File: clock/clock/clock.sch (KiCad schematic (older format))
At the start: 43 parts, among them J1 AVR-ISP-6, J10 Conn_01x05_Male, J11 Conn_01x05_Male, J12 Conn_01x05_Male, J13 Conn_01x05_Male, J2 EURORACK_CONN_10, J3 CV_IN, J4 CLOCK_OUT, J5 SUBDIV_OUT, J6 Conn_01x05_Female, J7 Conn_01x05_Female, J8 Conn_01x05_Female, J9 Conn_01x05_Female, SW1 SW_Push, SW2 SW_Push, SW3 SW_Rotary8, U1 ATmega328P-PU, U2 L7805, U3 SM460281N, U4 SM460281N, U5 SM460281N, Y1 16MHz

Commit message: pcb layout first pass
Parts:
- renumbered J13 to J10, J3 to J11, J4 to J12, J5 to J13, J6 to J3, J10 to J4, J7 to J5, J11 to J6, J8 to J7, J12 to J8
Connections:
- net +5V: now also J9.3 (Pin_3); no longer J7.4 (Pin_4)
- net AGND: now also J10.4 (Pin_4), R4.2, R5.2; no longer J13.S, J8.5 (Pin_5)
- net AVCC: now also J10.3 (Pin_3); no longer J8.4 (Pin_4)
- net B_CLOCK_OUT: now also J3.3 (Pin_3); no longer J3.1 (Pin_1)
- net B_CV_IN: now also J3.1 (Pin_1); no longer J3.3 (Pin_3)
- net B_LED0: now also J3.5 (Pin_5); no longer J3.4 (Pin_4)
- net B_LED1: now also J5.3 (Pin_3); no longer J3.5 (Pin_5)
- net B_LED3: now also J5.4 (Pin_4); no longer J5.2 (Pin_2)
- net B_LED4: now also J7.1 (Pin_1); no longer J5.3 (Pin_3)
- net B_LED5: now also J7.2 (Pin_2); no longer J5.4 (Pin_4)
- net B_LED6: now also J7.3 (Pin_3); no longer J5.5 (Pin_5)
- net B_LED_A: now also J7.4 (Pin_4); no longer J9.3 (Pin_3)
- net B_LED_B: now also J7.5 (Pin_5); no longer J9.4 (Pin_4)
- net B_LED_C1: now also J3.4 (Pin_4); no longer J7.1 (Pin_1)
- net B_LED_C2: now also J5.2 (Pin_2); no longer J7.2 (Pin_2)
- net B_LED_C3: now also J5.5 (Pin_5); no longer J7.3 (Pin_3)
- net CLOCK_OUT: now also J4.3 (Pin_3); no longer J4.1 (Pin_1)
- net CV_IN: now also J4.1 (Pin_1); no longer J4.3 (Pin_3)
- net GND: now also J9.4 (Pin_4); no longer J7.5 (Pin_5), R4.2, R5.2
- net LED0: now also U4.3 (G); no longer U4.4 (E)
- net LED1: now also U4.4 (E); no longer U4.2 (F)
- net LED2: now also U4.2 (F); no longer U4.3 (G)
- net LED_A: now also J8.4 (Pin_4); no longer J10.3 (Pin_3)
- net LED_B: now also J8.5 (Pin_5); no longer J10.4 (Pin_4)
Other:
- note added: "NOTE: this weird wiring is\nfor layout optimization"
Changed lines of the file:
@@
 $EndComp
 $Comp
-L Connector:AudioJack2 J4
+L Connector:AudioJack2 J12
 U 1 1 6321922B
 P 6750 5600
-F 0 "J4" H 6570 5583 50  0000 R CNN
+F 0 "J12" H 6570 5583 50  0000 R CNN
 F 1 "CLOCK_OUT" H 6570 5674 50  0000 R CNN
 F 2 "synth:Jack_3.5mm_QingPu_WQP-PJ398SM_Vertical_CircularHoles" H 6750 5600 50  0001 C CNN
@@
 $EndComp
 $Comp
-L Connector:AudioJack2 J5
+L Connector:AudioJack2 J13
 U 1 1 6321A6EF
 P 6750 6150
-F 0 "J5" H 6570 6133 50  0000 R CNN
+F 0 "J13" H 6570 6133 50  0000 R CNN
 F 1 "SUBDIV_OUT" H 6570 6224 50  0000 R CNN
 F 2 "synth:Jack_3.5mm_QingPu_WQP-PJ398SM_Vertical_CircularHoles" H 6750 6150 50  0001 C CNN
@@
 	1    0    0    -1
 $EndComp
-$Comp
-L power:GND #PWR015
-U 1 1 63227A93
-P 4100 6250
-F 0 "#PWR015" H 4100 6000 50  0001 C CNN
-F 1 "GND" H 4105 6077 50  0000 C CNN
-F 2 "" H 4100 6250 50  0001 C CNN
-F 3 "" H 4100 6250 50  0001 C CNN
-	1    4100 6250
-	1    0    0    -1
-$EndComp
 Wire Wire Line
 	4100 6250 4100 6100
@@
 	6850 2300 6850 1350
 Connection ~ 6850 1350
-Wire Wire Line
-	6750 1250 8400 1250
 Connection ~ 6750 1250
 Connection ~ 6650 1150
@@
 	11150 2500 11100 2500
 Wire Wire Line
-	8400 1250 10050 1250
-Wire Wire Line
 	8000 850  9650 850
 Connection ~ 8000 850
-Connection ~ 8400 1250
 Wire Wire Line
 	9500 2500 9500 2800
@@
 	1    0    0    -1
 $EndComp
-$Comp
-L power:GND #PWR018
-U 1 1 63552A08
-P 5250 6250
-F 0 "#PWR018" H 5250 6000 50  0001 C CNN
-F 1 "GND" H 5255 6077 50  0000 C CNN
-F 2 "" H 5250 6250 50  0001 C CNN
-F 3 "" H 5250 6250 50  0001 C CNN
-	1    5250 6250
-	1    0    0    -1
-$EndComp
 Wire Wire Line
 	5250 6250 5250 6100
@@
 B_SW2
 $Comp
-L Connector:AudioJack2 J3
+L Connector:AudioJack2 J11
 U 1 1 6328406C
 P 6750 5200
-F 0 "J3" H 6570 5183 50  0000 R CNN
+F 0 "J11" H 6570 5183 50  0000 R CNN
 F 1 "CV_IN" H 6570 5274 50  0000 R CNN
 F 2 "synth:Jack_3.5mm_QingPu_WQP-PJ398SM_Vertical_CircularHoles" H 6750 5200 50  0001 C CNN
@@
 	1000 2650 1250 2650
 $Comp
-L Connector:Conn_01x05_Male J10
+L Connector:Conn_01x05_Male J4
 U 1 1 63323658
 P 10200 3900
-F 0 "J10" H 10308 4281 50  0000 C CNN
+F 0 "J4" H 10308 4281 50  0000 C CNN
 F 1 "Conn_01x05_Male" V 10100 4000 50  0000 C CNN
 F 2 "Connector_PinHeader_2.54mm:PinHeader_1x05_P2.54mm_Vertical" H 10200 3900 50  0001 C CNN
@@
 $EndComp
 $Comp
-L Connector:Conn_01x05_Female J6
+L Connector:Conn_01x05_Female J3
 U 1 1 63325045
 P 9800 3900
-F 0 "J6" H 9650 4300 50  0000 L CNN
+F 0 "J3" H 9650 4300 50  0000 L CNN
 F 1 "Conn_01x05_Female" V 9850 3700 50  0000 L CNN
 F 2 "Connector_PinSocket_2.54mm:PinSocket_1x05_P2.54mm_Vertical" H 9800 3900 50  0001 C CNN
@@
 Text Label 2700 4150 0    50   ~ 0
 ~RESET
-Text Label 9500 6350 2    50   ~ 0
+Text Label 9450 5650 2    50   ~ 0
 B_LED_B
-Text Label 9500 4000 2    50   ~ 0
+Text Label 9500 4100 2    50   ~ 0
 B_LED0
-Text Label 9500 4100 2    50   ~ 0
+Text Label 9500 4650 2    50   ~ 0
 B_LED1
 Text Label 9500 4450 2    50   ~ 0
 B_LED2
-Text Label 9500 4550 2    50   ~ 0
+Text Label 9500 4750 2    50   ~ 0
 B_LED3
-Text Label 9500 4650 2    50   ~ 0
+Text Label 9500 5250 2    50   ~ 0
 B_LED4
-Text Label 9500 4750 2    50   ~ 0
+Text Label 9500 5350 2    50   ~ 0
 B_LED5
-Text Label 9500 4850 2    50   ~ 0
+Text Label 9500 5450 2    50   ~ 0
 B_LED6
 $Comp
 L power:+5V #PWR0101
 U 1 1 6334253F
-P 9000 5450
-F 0 "#PWR0101" H 9000 5300 50  0001 C CNN
-F 1 "+5V" H 9015 5623 50  0000 C CNN
-F 2 "" H 9000 5450 50  0001 C CNN
-F 3 "" H 9000 5450 50  0001 C CNN
-	1    9000 5450
+P 9050 6150
+F 0 "#PWR0101" H 9050 6000 50  0001 C CNN
+F 1 "+5V" H 9065 6323 50  0000 C CNN
+F 2 "" H 9050 6150 50  0001 C CNN
+F 3 "" H 9050 6150 50  0001 C CNN
+	1    9050 6150
 	1    0    0    -1
 $EndComp
@@
 L power:GND #PWR0102
 U 1 1 63342CA7
-P 9000 5750
-F 0 "#PWR0102" H 9000 5500 50  0001 C CNN
-F 1 "GND" H 9005 5577 50  0000 C CNN
-F 2 "" H 9000 5750 50  0001 C CNN
-F 3 "" H 9000 5750 50  0001 C CNN
-	1    9000 5750
+P 9050 6450
+F 0 "#PWR0102" H 9050 6200 50  0001 C CNN
+F 1 "GND" H 9055 6277 50  0000 C CNN
+F 2 "" H 9050 6450 50  0001 C CNN
+F 3 "" H 9050 6450 50  0001 C CNN
+	1    9050 6450
 	1    0    0    -1
 $EndComp
 Text Label 9500 6050 2    50   ~ 0
 B_KNOB
-Text Label 9500 3900 2    50   ~ 0
+Text Label 9500 3700 2    50   ~ 0
 B_CV_IN
-Text Label 9500 5250 2    50   ~ 0
+Text Label 9500 4000 2    50   ~ 0
 B_LED_C1
-Text Label 9500 5350 2    50   ~ 0
+Text Label 9500 4550 2    50   ~ 0
 B_LED_C2
-Text Label 9500 5450 2    50   ~ 0
+Text Label 9500 4850 2    50   ~ 0
 B_LED_C3
-Text Label 9500 6250 2    50   ~ 0
+Text Label 9450 5550 2    50   ~ 0
 B_LED_A
 Text Label 2700 2850 0    50   ~ 0
@@
 Text Label 9500 3800 2    50   ~ 0
 B_SUBDIV_OUT
-Text Label 9500 3700 2    50   ~ 0
+Text Label 9500 3900 2    50   ~ 0
 B_CLOCK_OUT
 $Comp
-L Connector:Conn_01x05_Male J11
+L Connector:Conn_01x05_Male J6
 U 1 1 633C2E72
 P 10200 4650
-F 0 "J11" H 10308 5031 50  0000 C CNN
+F 0 "J6" H 10308 5031 50  0000 C CNN
 F 1 "Conn_01x05_Male" V 10100 4750 50  0000 C CNN
 F 2 "Connector_PinHeader_2.54mm:PinHeader_1x05_P2.54mm_Vertical" H 10200 4650 50  0001 C CNN
@@
 $EndComp
 $Comp
-L Connector:Conn_01x05_Female J7
+L Connector:Conn_01x05_Female J5
 U 1 1 633C2E7C
 P 9800 4650
-F 0 "J7" H 9650 5050 50  0000 L CNN
+F 0 "J5" H 9650 5050 50  0000 L CNN
 F 1 "Conn_01x05_Female" V 9850 4450 50  0000 L CNN
 F 2 "Connector_PinSocket_2.54mm:PinSocket_1x05_P2.54mm_Vertical" H 9800 4650 50  0001 C CNN
@@
 $EndComp
 $Comp
-L Connector:Conn_01x05_Male J12
+L Connector:Conn_01x05_Male J8
 U 1 1 633ED584
 P 10200 5450
-F 0 "J12" H 10308 5831 50  0000 C CNN
+F 0 "J8" H 10308 5831 50  0000 C CNN
 F 1 "Conn_01x05_Male" V 10100 5550 50  0000 C CNN
 F 2 "Connector_PinHeader_2.54mm:PinHeader_1x05_P2.54mm_Vertical" H 10200 5450 50  0001 C CNN
@@
 $EndComp
 $Comp
-L Connector:Conn_01x05_Female J8
+L Connector:Conn_01x05_Female J7
 U 1 1 633ED58E
 P 9800 5450
-F 0 "J8" H 9650 5850 50  0000 L CNN
+F 0 "J7" H 9650 5850 50  0000 L CNN
 F 1 "Conn_01x05_Female" V 9850 5250 50  0000 L CNN
 F 2 "Connector_PinSocket_2.54mm:PinSocket_1x05_P2.54mm_Vertical" H 9800 5450 50  0001 C CNN
@@
 $EndComp
 $Comp
-L Connector:Conn_01x05_Male J13
+L Connector:Conn_01x05_Male J10
 U 1 1 633FDEA6
 P 10200 6250
-F 0 "J13" H 10308 6631 50  0000 C CNN
+F 0 "J10" H 10308 6631 50  0000 C CNN
 F 1 "Conn_01x05_Male" V 10100 6350 50  0000 C CNN
 F 2 "Connector_PinHeader_2.54mm:PinHeader_1x05_P2.54mm_Vertical" H 10200 6250 50  0001 C CNN
@@
 	9500 6450 9600 6450
 Wire Wire Line
-	9600 6350 9500 6350
-Wire Wire Line
-	9500 6250 9600 6250
-Wire Wire Line
-	9600 6150 9500 6150
-Wire Wire Line
 	9500 6050 9600 6050
 Wire Wire Line
-	9600 5650 9000 5650
-Wire Wire Line
-	9000 5650 9000 5750
-Wire Wire Line
-	9600 5550 9000 5550
-Wire Wire Line
-	9000 5550 9000 5450
+	9050 6350 9050 6450
+Wire Wire Line
+	9050 6250 9050 6150
 Wire Wire Line
 	9600 5450 9500 5450
@@
 Text Label 10500 5450 0    50   ~ 0
 LED6
-Text Label 10500 3900 0    50   ~ 0
+Text Label 10500 3700 0    50   ~ 0
 CV_IN
 Text Label 10500 3800 0    50   ~ 0
 SUBDIV_OUT
-Text Label 10500 3700 0    50   ~ 0
+Text Label 10500 3900 0    50   ~ 0
 CLOCK_OUT
-Text Label 10500 6350 0    50   ~ 0
+Text Label 10500 5650 0    50   ~ 0
 LED_B
 Text Label 10500 6050 0    50   ~ 0
 KNOB
-Text Label 10500 6250 0    50   ~ 0
+Text Label 10500 5550 0    50   ~ 0
 LED_A
 Text Label 10500 6150 0    50   ~ 0
@@
 Text Label 10500 4850 0    50   ~ 0
 LED_C3
-Text Label 10500 5550 0    50   ~ 0
+Text Label 10500 6250 0    50   ~ 0
 AVCC
 Text Label 6350 5700 2    50   ~ 0
@@
 Text Label 6250 3400 1    50   ~ 0
 AVCC
-Text Label 6350 6250 2    50   ~ 0
+Text Label 5250 6250 3    50   ~ 0
 AGND
 Text Label 7150 5300 0    50   ~ 0
@@
 	0    1    1    0
 $EndComp
-Text Label 10500 5650 0    50   ~ 0
+Text Label 10500 6350 0    50   ~ 0
 AGND
 $Comp
@@
 	8300 1150 9950 1150
 Wire Wire Line
-	6950 1450 8600 1450
-Wire Wire Line
-	6850 1350 8500 1350
-Wire Wire Line
 	8850 2400 8400 2400
 Wire Wire Line
-	8400 1250 8400 2400
-Wire Wire Line
 	8850 2300 8500 2300
 Wire Wire Line
-	8500 2300 8500 1350
-Connection ~ 8500 1350
-Wire Wire Line
-	8500 1350 10150 1350
+	6950 1450 8400 1450
 Wire Wire Line
 	8850 2200 8600 2200
 Wire Wire Line
-	8600 2200 8600 1450
-Connection ~ 8600 1450
-Wire Wire Line
-	8600 1450 10250 1450
+	8600 2200 8600 1350
+Connection ~ 8600 1350
+Wire Wire Line
+	8600 1350 10150 1350
+Wire Wire Line
+	6850 1350 8600 1350
+Wire Wire Line
+	6750 1250 8500 1250
+Wire Wire Line
+	8400 2400 8400 1450
+Connection ~ 8400 1450
+Wire Wire Line
+	8400 1450 10250 1450
+Wire Wire Line
+	8500 2300 8500 1250
+Connection ~ 8500 1250
+Wire Wire Line
+	8500 1250 10050 1250
+Text Notes 7950 800  0    50   ~ 0
+NOTE: this weird wiring is\nfor layout optimization
+Wire Wire Line
+	9050 6350 9600 6350
+Wire Wire Line
+	9450 5550 9600 5550
+Wire Wire Line
+	9600 5650 9450 5650
+Wire Wire Line
+	9500 6150 9600 6150
+Wire Wire Line
+	9050 6250 9600 6250
+Text Label 4100 6250 3    50   ~ 0
+AGND
 $EndSCHEMATC

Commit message: cleanup pcb and silkscreen
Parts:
- J11, J12, J13: symbol Connector:AudioJack2 -> synth:AudioJack_SwitchT
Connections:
- net AGND: now also J11.TN, J13.S
- no-connect marks 1 -> 3
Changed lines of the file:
@@
 $EndComp
 $Comp
-L Connector:AudioJack2 J12
+L synth:AudioJack_SwitchT J12
 U 1 1 6321922B
 P 6750 5600
@@
 $EndComp
 $Comp
-L Connector:AudioJack2 J13
+L synth:AudioJack_SwitchT J13
 U 1 1 6321A6EF
-P 6750 6150
-F 0 "J13" H 6570 6133 50  0000 R CNN
-F 1 "SUBDIV_OUT" H 6570 6224 50  0000 R CNN
-F 2 "synth:Jack_3.5mm_QingPu_WQP-PJ398SM_Vertical_CircularHoles" H 6750 6150 50  0001 C CNN
-F 3 "~" H 6750 6150 50  0001 C CNN
-	1    6750 6150
+P 6750 6000
+F 0 "J13" H 6570 5983 50  0000 R CNN
+F 1 "SUBDIV_OUT" H 6570 6074 50  0000 R CNN
+F 2 "synth:Jack_3.5mm_QingPu_WQP-PJ398SM_Vertical_CircularHoles" H 6750 6000 50  0001 C CNN
+F 3 "~" H 6750 6000 50  0001 C CNN
+	1    6750 6000
 	-1   0    0    1
 $EndComp
@@
 Text Label 6350 5600 2    50   ~ 0
 CLOCK_OUT
-Text Label 6350 6150 2    50   ~ 0
+Text Label 6350 6000 2    50   ~ 0
 SUBDIV_OUT
 Wire Wire Line
-	6350 6150 6550 6150
+	6350 6000 6550 6000
 Wire Wire Line
 	6350 5600 6550 5600
@@
 B_SW2
 $Comp
-L Connector:AudioJack2 J11
+L synth:AudioJack_SwitchT J11
 U 1 1 6328406C
 P 6750 5200
@@
 Text Label 10500 6250 0    50   ~ 0
 AVCC
-Text Label 6350 5700 2    50   ~ 0
+Text Label 6350 6100 2    50   ~ 0
 AGND
 Wire Wire Line
@@
 AVCC
 Wire Wire Line
-	6350 6250 6550 6250
+	6350 6100 6550 6100
 Wire Wire Line
 	6350 5700 6550 5700
@@
 Text Label 4100 6250 3    50   ~ 0
 AGND
+Text Label 6350 5700 2    50   ~ 0
+AGND
+NoConn ~ 6550 5900
+NoConn ~ 6550 5500
+Text Label 7150 5100 0    50   ~ 0
+AGND
+Wire Wire Line
+	7150 5100 6950 5100
 $EndSCHEMATC

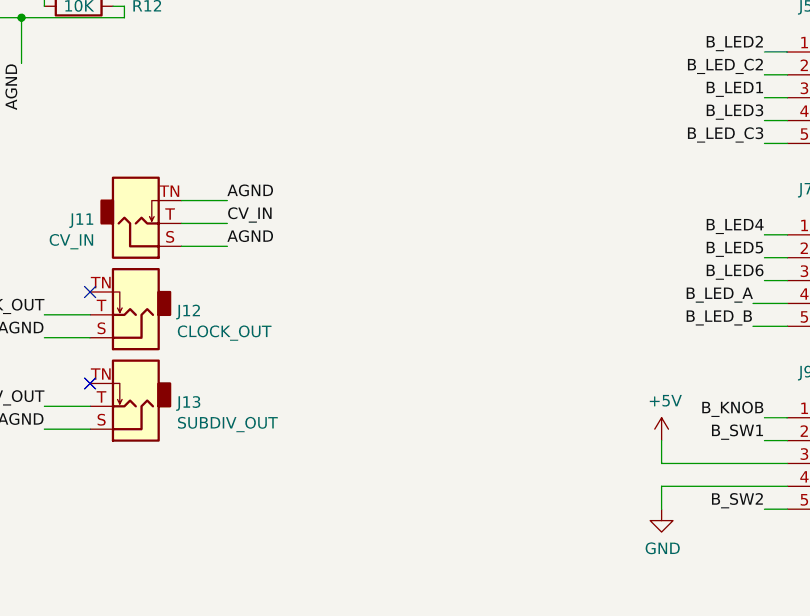
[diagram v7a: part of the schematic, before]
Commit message: analog input pin protection
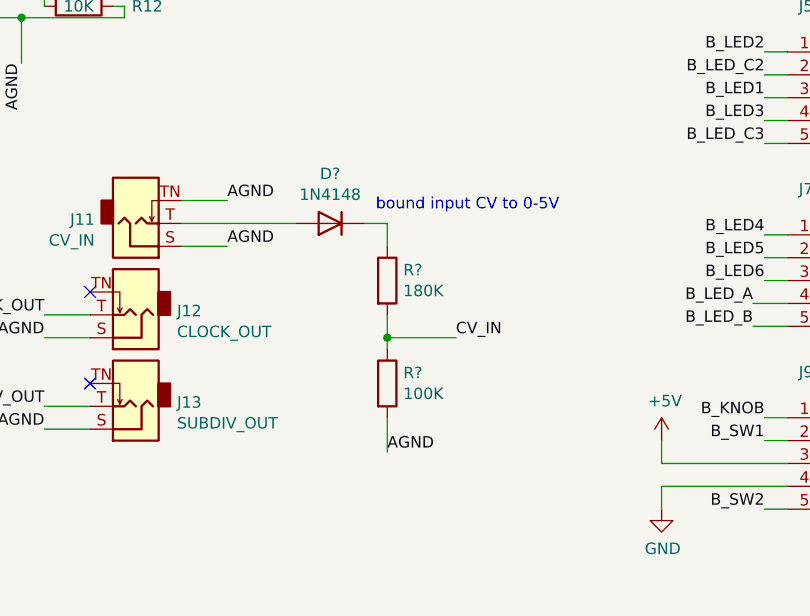
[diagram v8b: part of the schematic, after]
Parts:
- added D?: 1N4148, Diode_THT:D_DO-35_SOD27_P7.62mm_Horizontal, symbol Diode:1N4148
- added R?: 180K, symbol Device:R
- added R?: 100K, symbol Device:R
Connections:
- net AGND: now also R?.2
- net CV_IN: now also R?.1, R?.2; no longer J11.T
- new net: D?.2 (A), J11.T
- new net: D?.1 (K), R?.1
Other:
- note added: "bound input CV to 0-5V"
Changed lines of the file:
@@
 	1    0    0    1
 $EndComp
-Text Label 7150 5200 0    50   ~ 0
+Text Label 8150 5700 0    50   ~ 0
 CV_IN
-Wire Wire Line
-	7150 5200 6950 5200
 Text Label 2700 3650 0    50   ~ 0
 B_CV_IN
@@
 Text Label 5250 6250 3    50   ~ 0
 AGND
-Text Label 7150 5300 0    50   ~ 0
+Text Label 7850 6200 0    50   ~ 0
 AGND
 Text Label 5250 5200 1    50   ~ 0
@@
 Wire Wire Line
 	7150 5100 6950 5100
+$Comp
+L Diode:1N4148 D?
+U 1 1 6342DA40
+P 7600 5200
+F 0 "D?" H 7600 4983 50  0000 C CNN
+F 1 "1N4148" H 7600 5074 50  0000 C CNN
+F 2 "Diode_THT:D_DO-35_SOD27_P7.62mm_Horizontal" H 7600 5025 50  0001 C CNN
+F 3 "https://assets.nexperia.com/documents/data-sheet/1N4148_1N4448.pdf" H 7600 5200 50  0001 C CNN
+	1    7600 5200
+	-1   0    0    1
+$EndComp
+$Comp
+L Device:R R?
+U 1 1 6342F08D
+P 7850 5450
+F 0 "R?" H 7920 5496 50  0000 L CNN
+F 1 "180K" H 7920 5405 50  0000 L CNN
+F 2 "" V 7780 5450 50  0001 C CNN
+F 3 "~" H 7850 5450 50  0001 C CNN
+	1    7850 5450
+	1    0    0    -1
+$EndComp
+$Comp
+L Device:R R?
+U 1 1 6342F86A
+P 7850 5900
+F 0 "R?" H 7920 5946 50  0000 L CNN
+F 1 "100K" H 7920 5855 50  0000 L CNN
+F 2 "" V 7780 5900 50  0001 C CNN
+F 3 "~" H 7850 5900 50  0001 C CNN
+	1    7850 5900
+	1    0    0    -1
+$EndComp
+Wire Wire Line
+	7850 6200 7850 6050
+Wire Wire Line
+	7850 5750 7850 5700
+Wire Wire Line
+	7850 5300 7850 5200
+Wire Wire Line
+	7850 5200 7750 5200
+Wire Wire Line
+	6950 5200 7450 5200
+Wire Wire Line
+	8150 5700 7850 5700
+Connection ~ 7850 5700
+Wire Wire Line
+	7850 5700 7850 5600
+Text Label 7150 5300 0    50   ~ 0
+AGND
+Text Notes 7800 5150 0    50   ~ 0
+bound input CV to 0-5V
 $EndSCHEMATC
